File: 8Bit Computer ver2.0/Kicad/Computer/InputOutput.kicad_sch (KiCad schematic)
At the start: 131 parts, among them IC236 SN74F521DWR, IC237 SN74F521DWR, IC238 DS1100Z-150+, IC239 SN74LVC1G14DBVR, IC240 SN74LVC1G86DBVR, IC241 SN74LVC1G14DBVR, IC242 SN74F521DWR, IC243 SN74F521DWR, IC244 SN74LVC1G14DBVR, IC245 SN74LVC1G14DBVR, IC246 SN74LVC1G14DBVR, IC247 SN74ABT574ADWR, IC248 SN74LVC1G14DBVR, IC249 SN74LVC1G14DBVR, IC250 SN74AHC74DR, IC251 SN74LVC1G08DBVR, IC252 SN74LVC1G14DBVR, IC253 SN74AHC74DR, IC254 SN74AHC74DR, IC255 SN74ABT574ADWR, IC256 SN74ABT245BDWR, IC257 SN74AHC74DR, IC258 SN74LVC1G08DBVR, IC259 SN74ABT245BDWR, IC260 SN74ABT245BDWR, IC261 MP2338GTL-Z, IC262 SN74AHC540DWR, IC263 SN74AHC540DWR

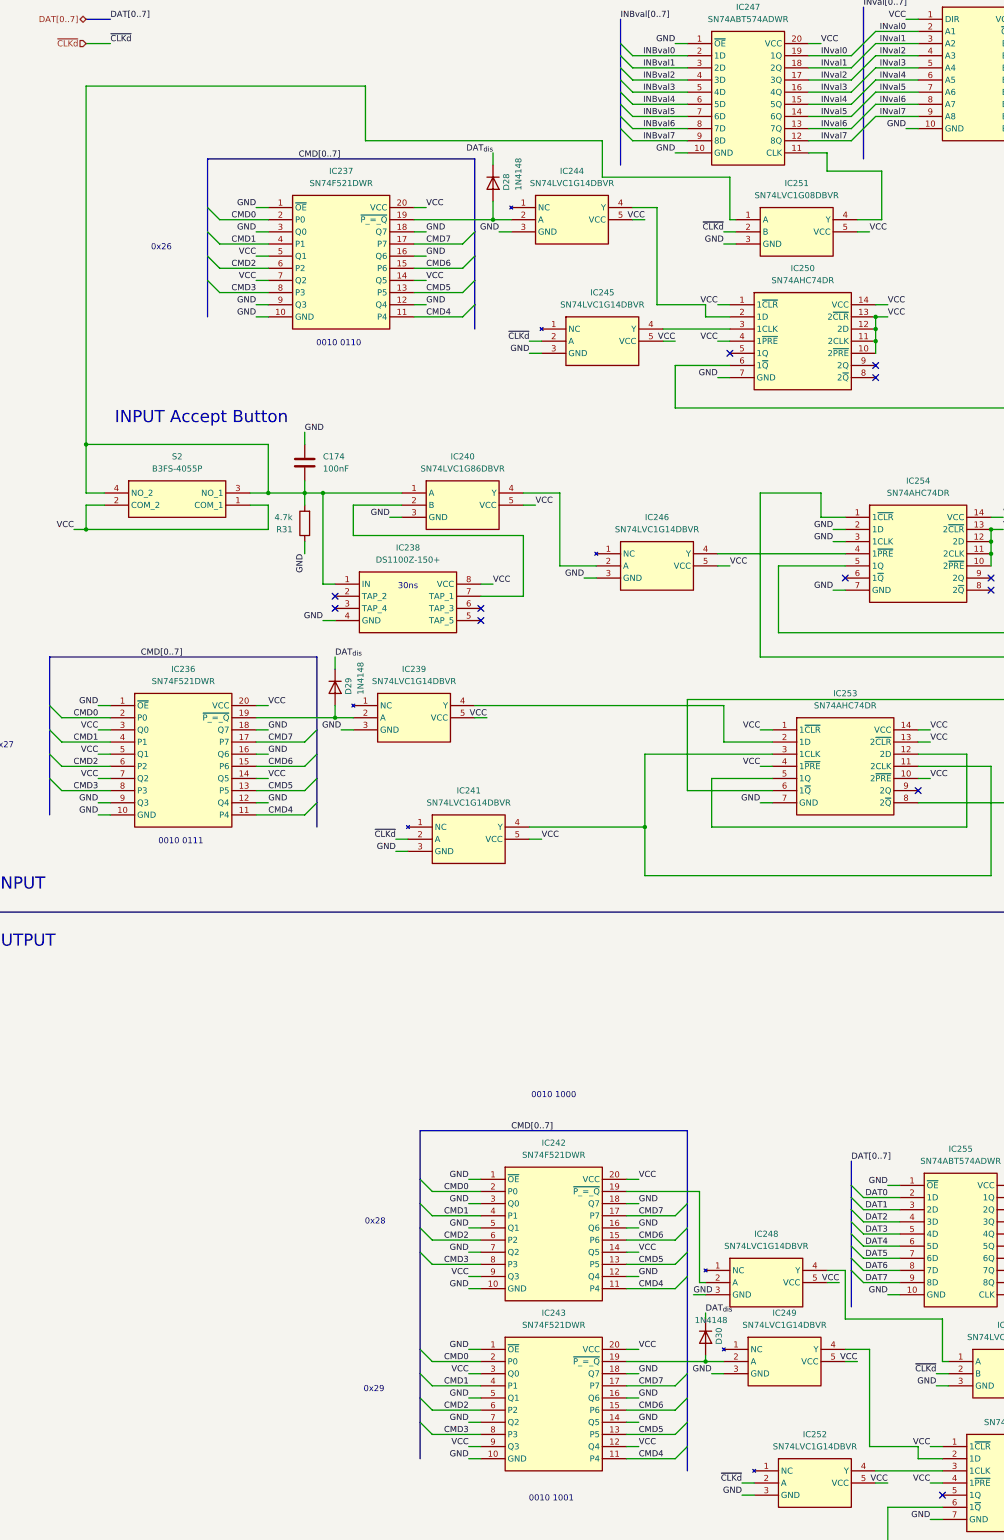
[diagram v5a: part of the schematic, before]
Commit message: Kicad,parts
parts:
added 1N4148 Diode SMD
Kicad:
fixed some routings of Schematic
created Flash mem and RAM PCB
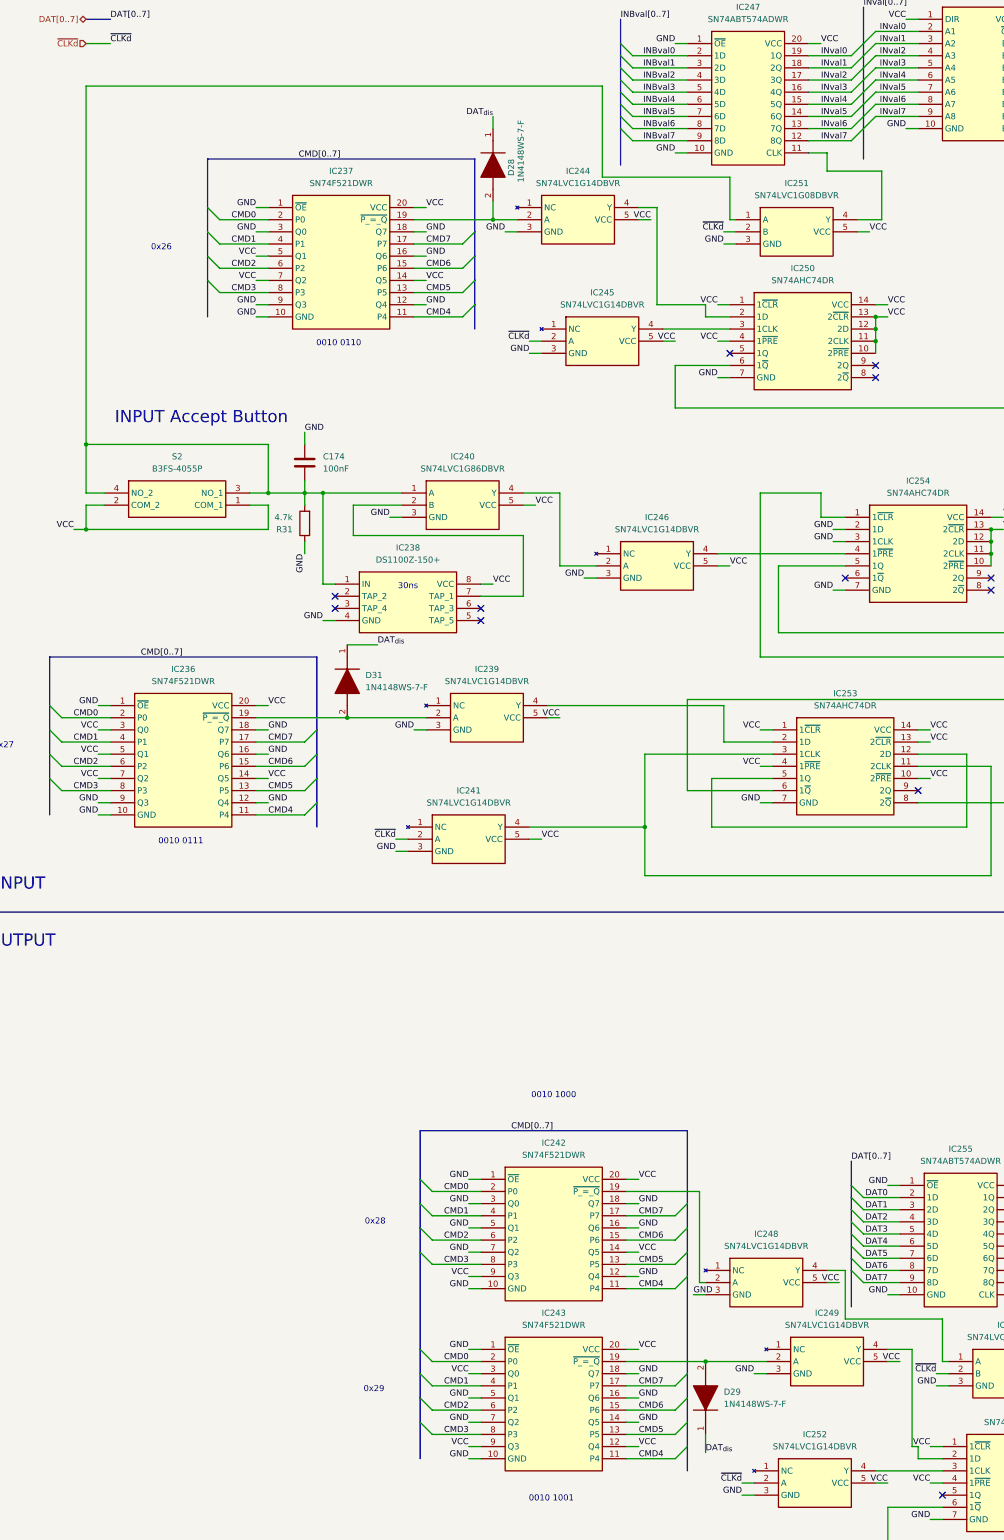
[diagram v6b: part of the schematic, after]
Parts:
- removed D28, D29, D30: 1N4148, Diode_THT:D_DO-35_SOD27_P10.16mm_Horizontal, symbol Diode:1N4148
- added D28, D29, D31: 1N4148WS-7-F, Samacsys:SOD2513X120N, symbol Samacsys:1N4148WS-7-F
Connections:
- net DAT_{dis}: now also D28.1 (K), D29.1 (K), D31.1 (K)
- net at IC237.19 (~{P_=_Q}), IC244.2 (A): now also D28.2 (A)
- net at IC236.19 (~{P_=_Q}), IC239.2 (A): now also D31.2 (A)
- net at IC243.19 (~{P_=_Q}), IC249.2 (A): now also D29.2 (A)
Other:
- moved on the sheet: IC239, IC244, IC249

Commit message: Kicad
added 10pin 2,54mm Header
finished ALU PCB and added pin Header for extra use (DAT,ADR,CMD,Ddis,CLK)
31.12-06.01 about +60hr for ALU
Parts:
- added C307, C308, C309: 100nF, Capacitor_SMD:C_1206_3216Metric_Pad1.33x1.80mm_HandSolder, symbol Device:C
- added IC102: SN74LVC1G32DBVR, Samacsys:SOT95P280X145-5N, symbol Samacsys:SN74LVC1G32DBVR
- added IC272: SN74F521DWR, Samacsys:SOIC127P1030X265-20N, symbol Samacsys:SN74F521DWR
- added IC273: SN74LVC1G14DBVR, Samacsys:SOT95P280X145-5N, symbol Samacsys:SN74LVC1G14DBVR
- added LED17, LED18, LED19, LED20, LED21: LTST-C170KFKT, Samacsys:LEDC2012X120N, symbol Samacsys:LTST-C170KFKT
- added R72, R73, R74, R75, R76: 150, Resistor_SMD:R_1206_3216Metric_Pad1.30x1.75mm_HandSolder, symbol Device:R
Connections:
- net CMD0: now also IC272.2 (P0)
- net CMD1: now also IC272.4 (P1)
- net CMD2: now also IC272.6 (P2)
- net CMD3: now also IC272.8 (P3)
- net CMD4: now also IC272.11 (P4)
- net CMD5: now also IC272.13 (P5)
- net CMD6: now also IC272.15 (P6)
- net CMD7: now also IC272.17 (P7)
- net GND: now also IC237.5 (Q1), IC237.7 (Q2), C307.1, C308.1, C309.1, IC102.3 (GND), IC272.1 (~{OE}), IC272.10 (GND), IC272.12 (Q4), IC272.16 (Q6), IC272.18 (Q7), IC272.3 (Q0), IC272.9 (Q3), IC273.3 (GND); no longer IC237.9 (Q3)
- net VCC: now also IC237.9 (Q3), C307.2, C308.2, C309.2, IC102.5 (VCC), IC272.14 (Q5), IC272.20 (VCC), IC272.5 (Q1), IC272.7 (Q2), IC273.5 (VCC), R72.1, R73.1, R74.1, R75.1, R76.1; no longer IC237.5 (Q1), IC237.7 (Q2)
- net at C174.1, IC238.1 (IN), IC240.1 (A)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: now also IC102.2 (B); no longer IC251.1 (A)
- net at D29.2 (A), IC249.2 (A): now also IC237.19 (~{P_=_Q}), LED20.1 (K); no longer IC243.19 (~{P_=_Q})
- net at D31.2 (A), IC239.2 (A): now also IC242.19 (~{P_=_Q}), LED17.1 (K); no longer IC236.19 (~{P_=_Q})
- net at D28.2 (A), IC244.2 (A): now also IC236.19 (~{P_=_Q}), LED18.1 (K); no longer IC237.19 (~{P_=_Q})
- net at IC248.2 (A): now also IC243.19 (~{P_=_Q}), LED19.1 (K); no longer IC242.19 (~{P_=_Q})
- new net: IC272.19 (~{P_=_Q}), IC273.2 (A), LED21.1 (K)
- new net: LED21.2 (A), R76.2
- new net: IC102.4 (Y), IC251.1 (A)
- new net: IC102.1 (A), IC273.4 (Y)
- new net: LED20.2 (A), R75.2
- new net: LED19.2 (A), R74.2
- new net: LED17.2 (A), R72.2
- new net: LED18.2 (A), R73.2
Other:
- note added: "0010 1010"
- note added: "0x2A"
- moved on the sheet: C175, C176, C177, C178, C179, C180, C182, C214, C215, C216, D28, IC236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

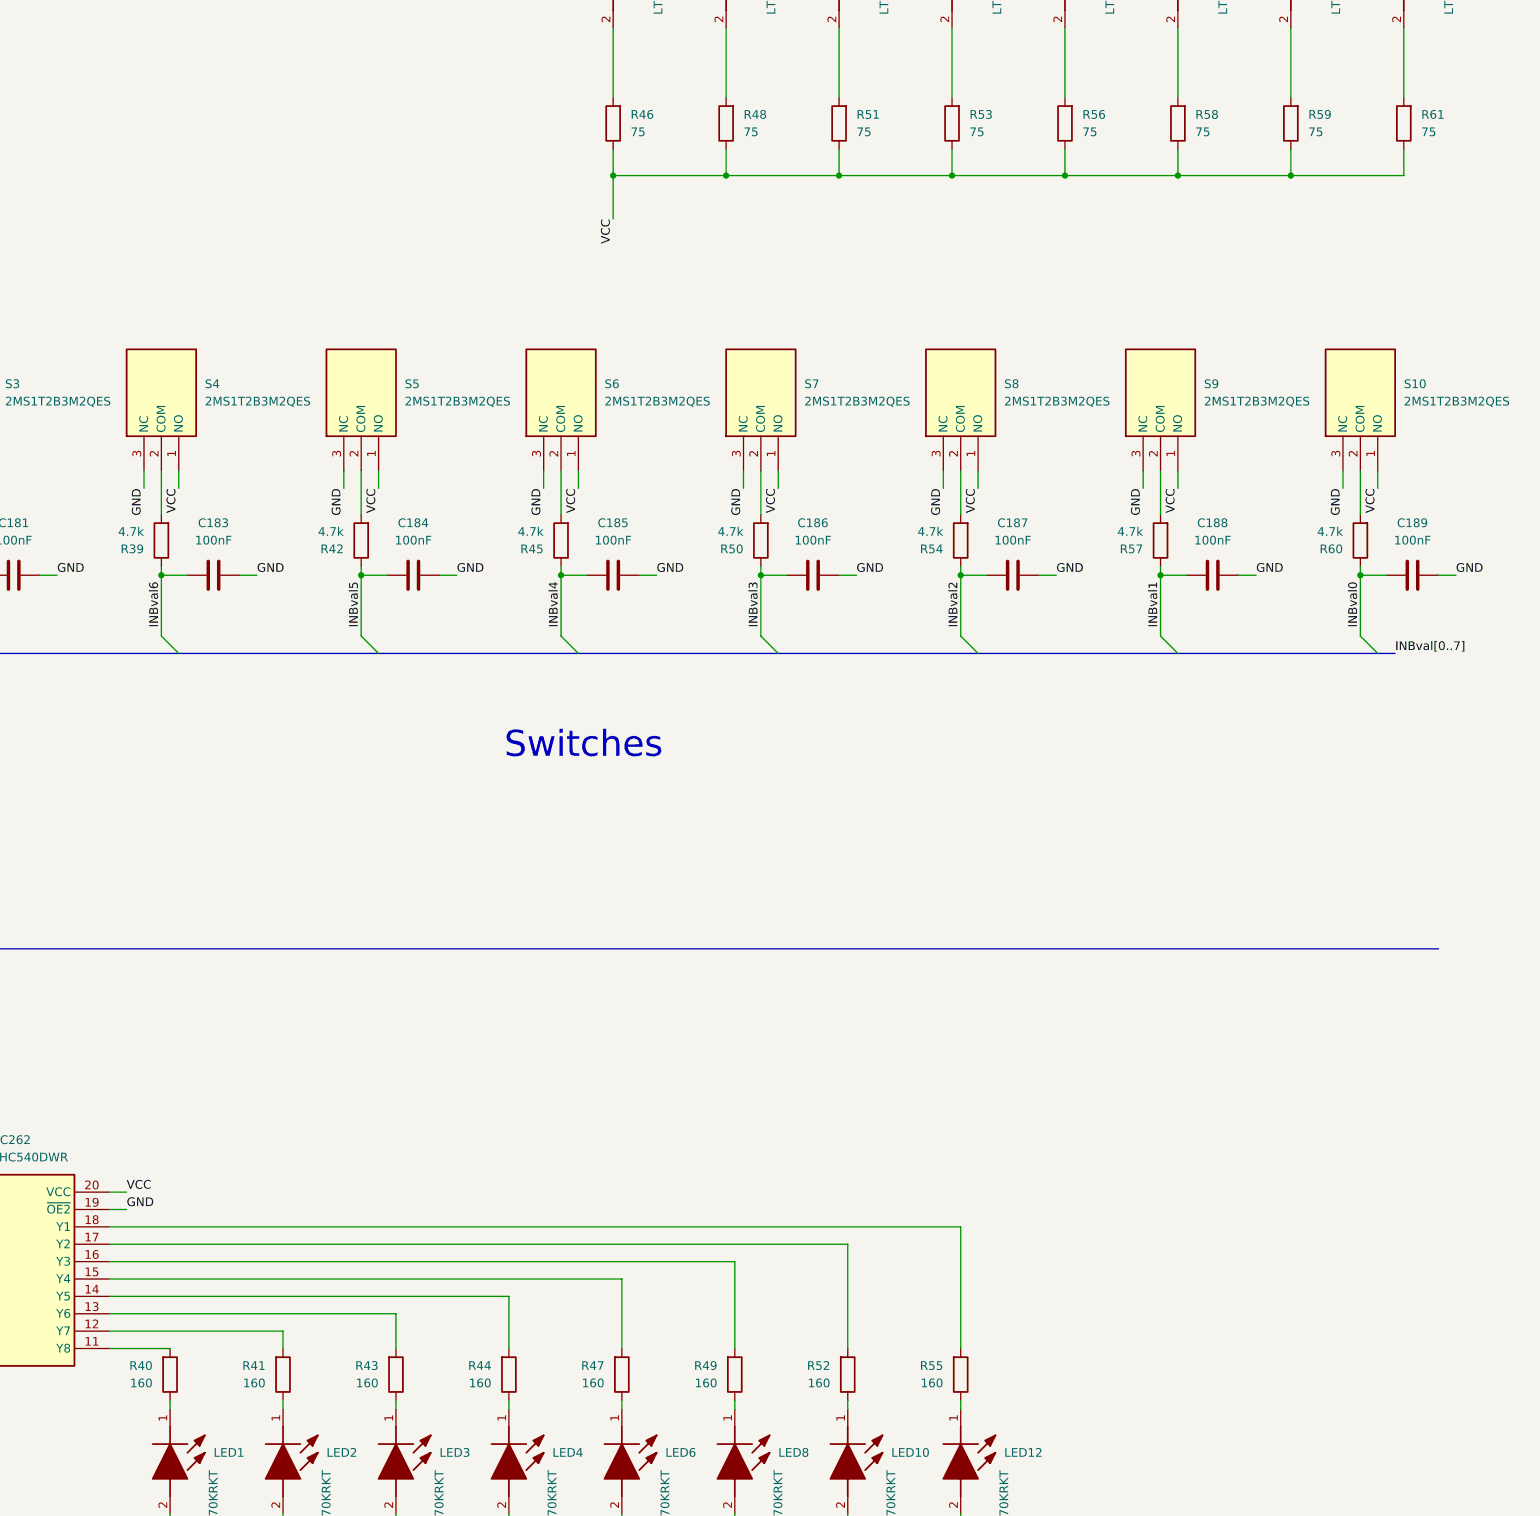
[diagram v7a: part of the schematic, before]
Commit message: Kicad Fixes only schematic
fixed important schematic errors
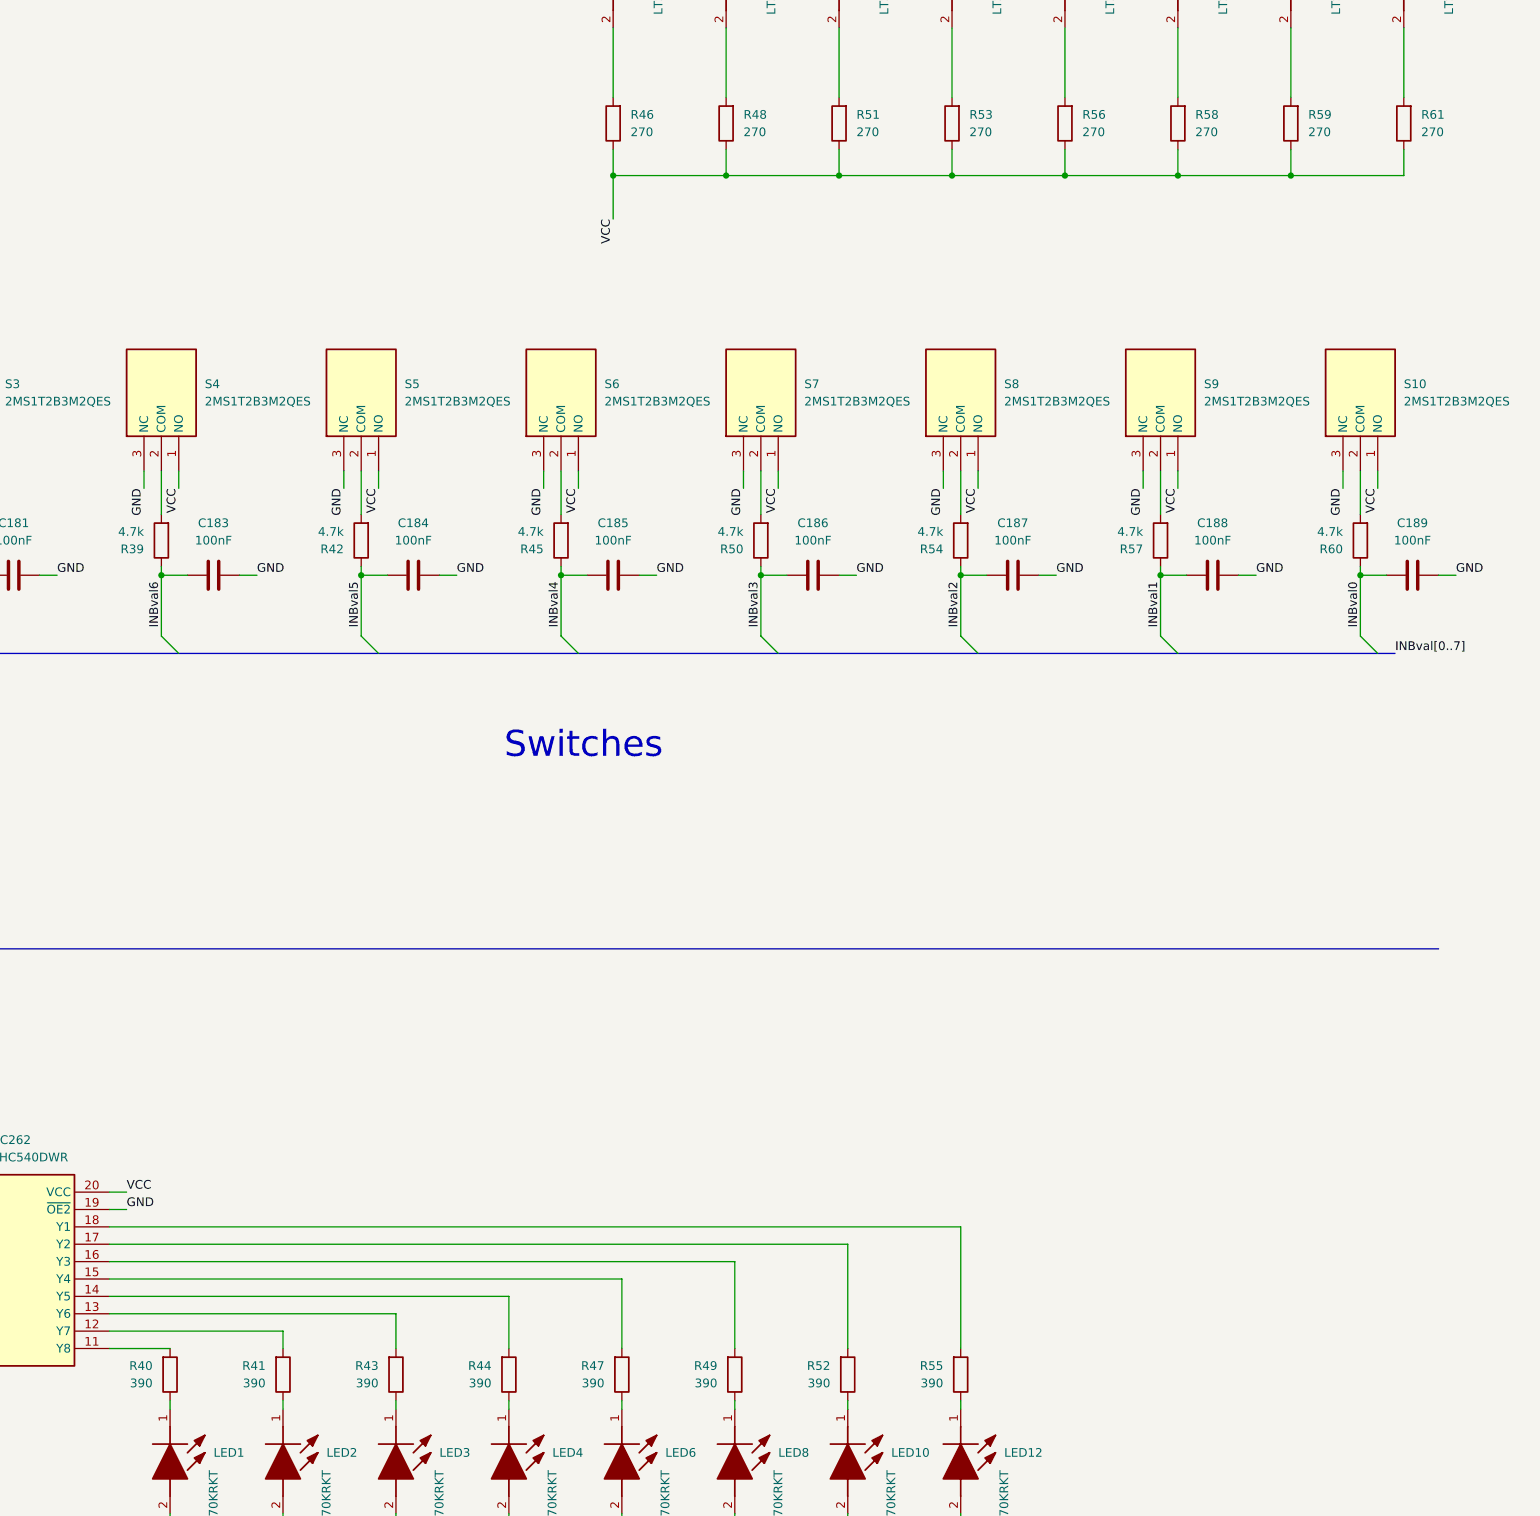
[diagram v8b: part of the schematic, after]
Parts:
- R40, R41, R43, R44, R47, R49, R52, R55: value 160 -> 390
- R46, R48, R51, R53, R56, R58, R59, R61: value 75 -> 270
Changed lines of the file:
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@@
 			)
 		)
-		(property "Value" "75"
+		(property "Value" "270"
 			(at 449.58 132.0799 0)
 			(effects
@@
 			)
 		)
-		(property "Value" "160"
+		(property "Value" "390"
 			(at 478.79 314.9599 0)
 			(effects
@@
 			)
 		)
-		(property "Value" "160"
+		(property "Value" "390"
 			(at 396.24 314.9599 0)
 			(effects
@@
 			)
 		)
-		(property "Value" "160"
+		(property "Value" "390"
 			(at 412.75 314.9599 0)
 			(effects
@@
 			)
 		)
-		(property "Value" "75"
+		(property "Value" "270"
 			(at 548.64 132.0799 0)
 			(effects
@@
 			)
 		)
-		(property "Value" "75"
+		(property "Value" "270"
 			(at 466.09 132.0799 0)
 			(effects
@@
 			)
 		)
-		(property "Value" "160"
+		(property "Value" "390"
 			(at 495.3 314.9599 0)
 			(effects
@@
 			)
 		)
-		(property "Value" "160"
+		(property "Value" "390"
 			(at 462.28 314.9599 0)
 			(effects
@@
 			)
 		)
-		(property "Value" "75"
+		(property "Value" "270"
 			(at 565.15 132.0799 0)
 			(effects
@@
 			)
 		)
-		(property "Value" "75"
+		(property "Value" "270"
 			(at 515.62 132.0799 0)
 			(effects
@@
 			)
 		)
-		(property "Value" "160"
+		(property "Value" "390"
 			(at 379.73 314.9599 0)
 			(effects
@@
 			)
 		)
-		(property "Value" "75"
+		(property "Value" "270"
 			(at 532.13 132.0799 0)
 			(effects
@@
 			)
 		)
-		(property "Value" "75"
+		(property "Value" "270"
 			(at 499.11 132.0799 0)
 			(effects
@@
 			)
 		)
-		(property "Value" "160"
+		(property "Value" "390"
 			(at 445.77 314.9599 0)
 			(effects
@@
 			)
 		)
-		(property "Value" "160"
+		(property "Value" "390"
 			(at 429.26 314.9599 0)
 			(effects
@@
 			)
 		)
-		(property "Value" "75"
+		(property "Value" "270"
 			(at 482.6 132.0799 0)
 			(effects
